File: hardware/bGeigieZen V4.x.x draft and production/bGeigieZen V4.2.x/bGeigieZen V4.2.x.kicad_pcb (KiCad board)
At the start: 2 copper layers, 129.4 x 64.6 mm, 13 parts, among them J1 M5 2x15 pin, J3 GPS, J4 Geiger Safepulse, J5 Extra support header

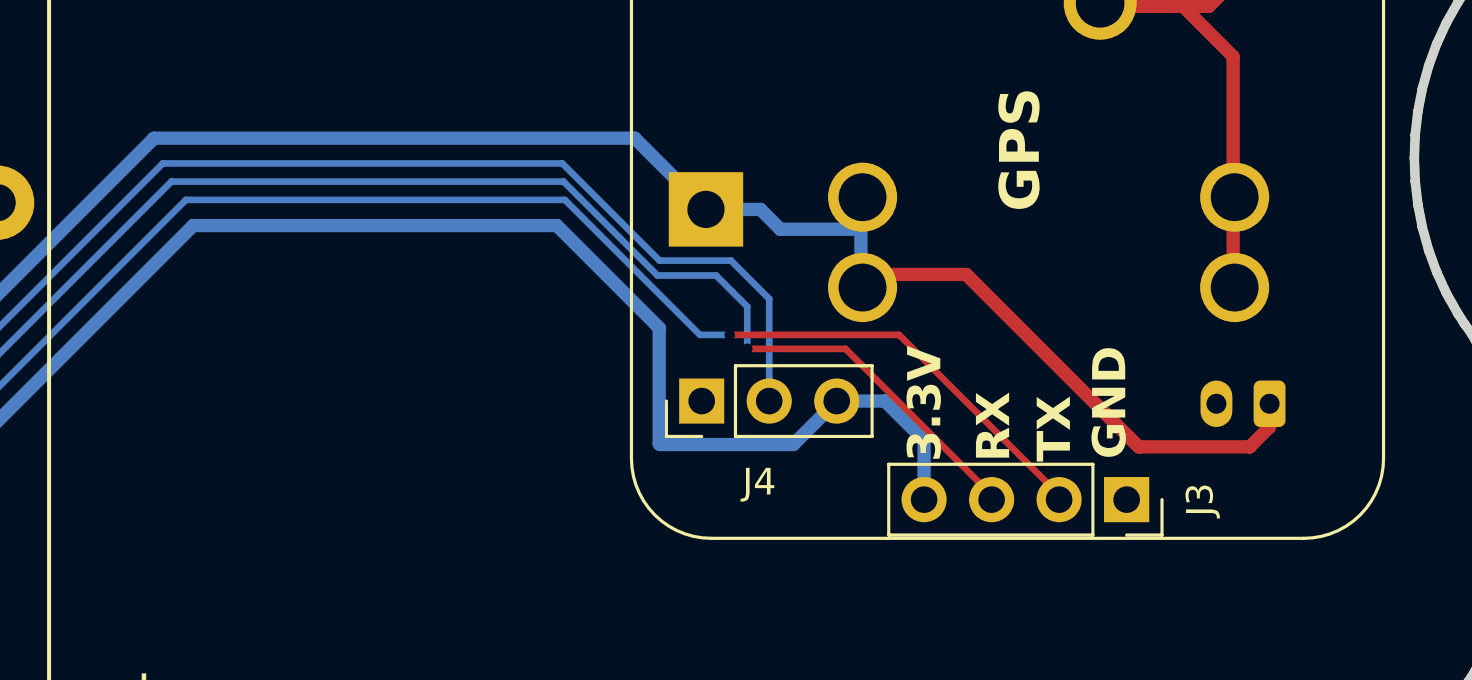
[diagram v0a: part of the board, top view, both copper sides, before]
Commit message: chore: update bGeigieZen V4.2.2 PCB to KiCad 10 and refine properties
Update the bGeigieZen V4.2.x PCB design to KiCad version 10.0, bumping the revision to V4.2.2. The update includes migrating the file format to the new version 20260206 standard and restructuring layer settings for tenting, covering, and plugging. Additionally, component properties have been standardized to hide names and disable autoplace, while removing obsolete HPGL plot parameters and updating the project context for better BOM and position file generation.
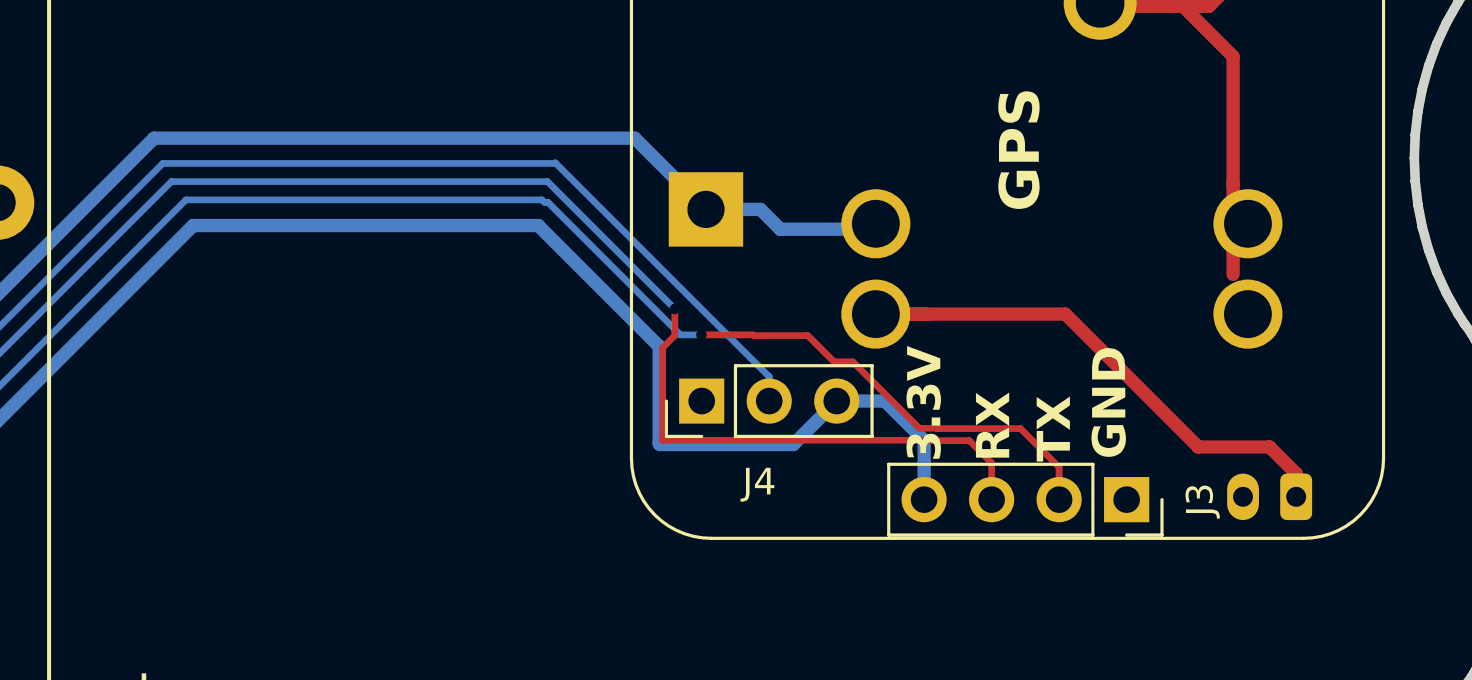
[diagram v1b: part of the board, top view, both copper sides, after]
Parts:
- moved QI-charger 3.64 mm to (206.7, 98.6)
- moved Fuse 2A 1.12 mm to (197.9, 90.0)
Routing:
- net /RX2: track 80.5 -> 84.0 mm
- net /GIO2 on Core and GIO32 on Core-2: track 79.2 -> 77.6 mm
- net /BAT: track 112.3 -> 110.7 mm
- net /TX2: track 83.6 -> 84.4 mm
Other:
- board text added: "bGeigieZen V4.2.2"

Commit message: V4.2.2
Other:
- board text removed: "bGeigieZen V4.2.1"
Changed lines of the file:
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@@
 		)
 	)
-	(gr_text "bGeigieZen V4.2.1\n\n"
+	(gr_text "bGeigieZen V4.2.2\n\n"
 		(at 163.9316 124.2048 90)
 		(layer "F.SilkS")

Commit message: chore: update bGeigieZen to V4.3.0 and add support headers
Bump hardware revision from V4.2.2 to V4.3.0 in the KiCad PCB title block.
Update the submodule reference to the latest commit.
Add new 2-pin header connectors (J4, J5) for extra support functionality.
Rename existing connector pins to avoid duplicate numbering conflicts.
Replace generic ground symbols with standard male pin headers for J4 and J5.
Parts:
- removed Fuse 2A: Fuse_Small, bGeigieZen:FUSE_3557-2
- added F2: Polyfuse, Connector_PinHeader_2.54mm:PinHeader_2x01_P2.54mm_Vertical, B.Cu at (203.6, 89.8)
- renumbered D1 to D2
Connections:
- BT1 pad 1: GND -> Net-(BT1-+)
- BT1 pad PWR@2: GND -> (no net)
- BT1 pad PWR@3: GND -> (no net)
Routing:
- net /BAT: track 110.7 -> 112.0 mm
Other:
- board text added: "bGeigieZen V4.3.0"
- board text removed: "bGeigieZen V4.2.2"

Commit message: Thicker traces for the power to the diode.
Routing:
- net Net-(BT1-+): track 25.0 -> 26.3 mm
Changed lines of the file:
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@@
 		(start 197.5626 89.825)
 		(end 201.0626 89.825)
-		(width 0.5)
+		(width 1)
 		(layer "F.Cu")
 		(net "/BAT")
@@
 		(start 195.5216 87.784)
 		(end 197.5626 89.825)
-		(width 0.5)
+		(width 1)
 		(layer "F.Cu")
 		(net "/BAT")
@@
 		(start 184.4776 87.784)
 		(end 195.5216 87.784)
-		(width 0.5)
+		(width 1)
 		(layer "F.Cu")
 		(net "/BAT")
@@
 	)
 	(segment
+		(start 197.936 76.3216)
+		(end 197.936 79.228414)
+		(width 1)
+		(layer "F.Cu")
+		(net "Net-(BT1-+)")
+	)
+	(segment
 		(start 202.4195 80.1419)
 		(end 201.9195 80.1419)
@@
 		(start 204.3076 86.83)
 		(end 204.3076 82.03)
-		(width 0.5)
+		(width 1)
+		(layer "F.Cu")
+		(net "Net-(BT1-+)")
+	)
+	(segment
+		(start 199.3076 74.95)
+		(end 197.936 76.3216)
+		(width 1)
 		(layer "F.Cu")
 		(net "Net-(BT1-+)")
@@
 		(start 203.6026 87.535)
 		(end 204.3076 86.83)
-		(width 0.5)
-		(layer "F.Cu")
-		(net "Net-(BT1-+)")
-	)
-	(segment
-		(start 198.9876 78.8658)
-		(end 198.9876 73.7858)
-		(width 0.5)
+		(width 1)
 		(layer "F.Cu")
 		(net "Net-(BT1-+)")
@@
 		(start 202.4195 80.1419)
 		(end 200.2637 80.1419)
-		(width 0.5)
+		(width 1)
 		(layer "F.Cu")
 		(net "Net-(BT1-+)")
@@
 		(start 202.4195 80.1419)
 		(end 203.4037 80.1419)
-		(width 0.5)
+		(width 1)
 		(layer "F.Cu")
 		(net "Net-(BT1-+)")
@@
 		(start 203.6026 89.825)
 		(end 203.6026 87.535)
-		(width 0.5)
+		(width 1)
 		(layer "F.Cu")
 		(net "Net-(BT1-+)")
@@
 		(start 203.4037 80.1419)
 		(end 206.0556 77.49)
-		(width 0.5)
+		(width 1)
+		(layer "F.Cu")
+		(net "Net-(BT1-+)")
+	)
+	(segment
+		(start 197.936 79.228414)
+		(end 199.0137 80.306114)
+		(width 1)
 		(layer "F.Cu")
 		(net "Net-(BT1-+)")
@@
 		(start 204.3076 82.03)
 		(end 202.4195 80.1419)
-		(width 0.5)
+		(width 1)
 		(layer "F.Cu")
 		(net "Net-(BT1-+)")
